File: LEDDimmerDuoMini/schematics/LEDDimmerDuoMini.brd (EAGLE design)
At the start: 84.8 x 27.9 mm, 17 parts, among them IC1 7805T, T1 2N3904, T2 2N3904

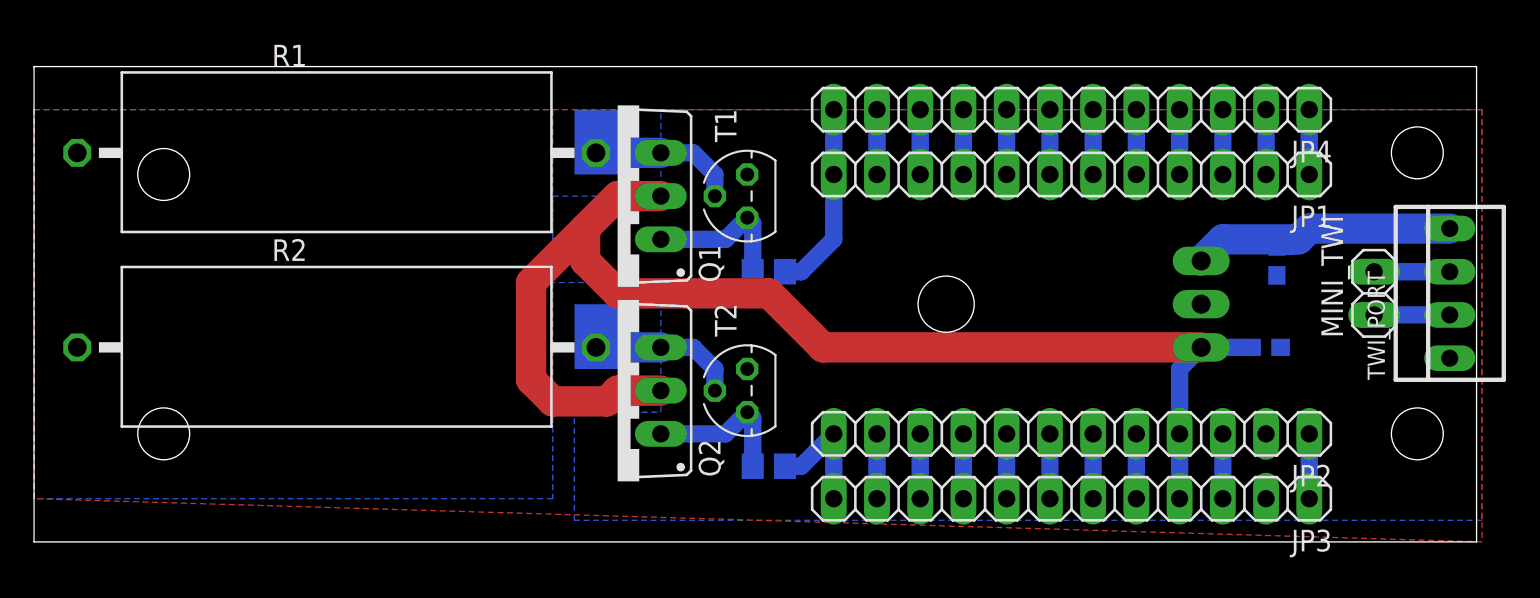
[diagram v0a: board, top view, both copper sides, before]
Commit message: Fixed faulty scematic for LEDDimmerDuoMini
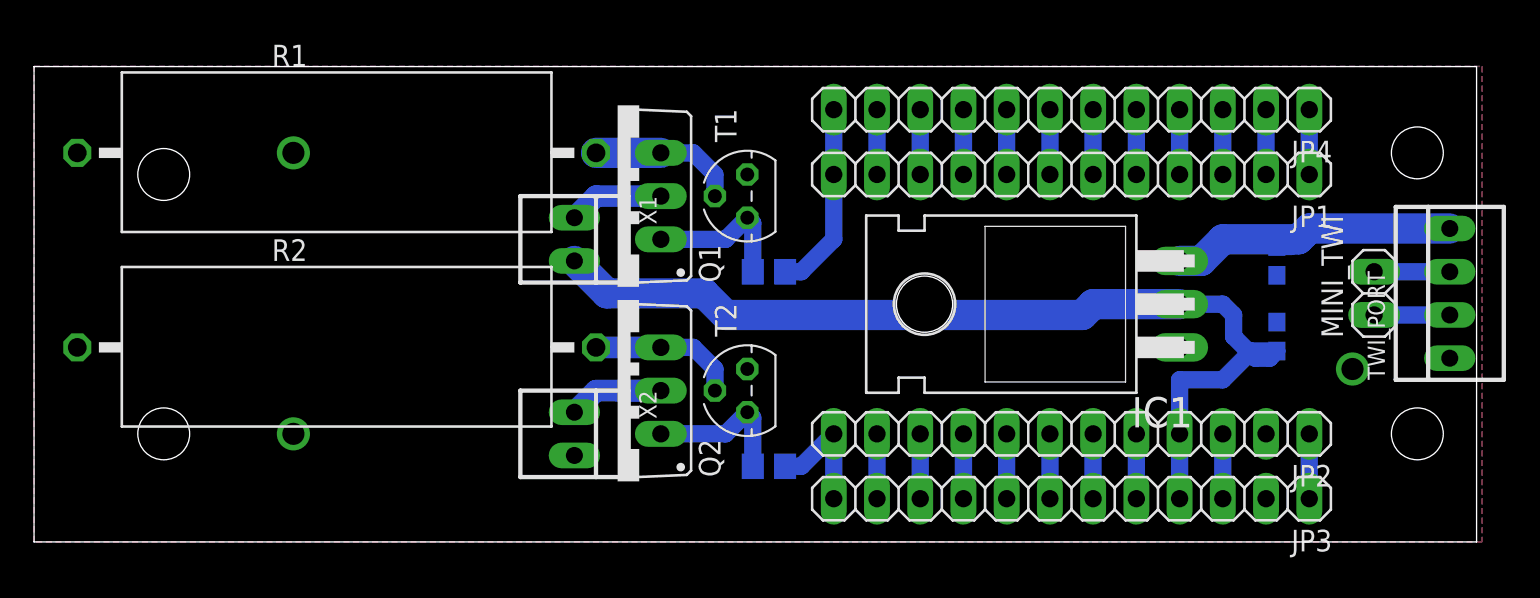
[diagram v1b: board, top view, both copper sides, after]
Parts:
- added X1, X2: 22-23-2021, con-molex:22-23-2021
- IC1: device adafruit:TO220H -> linear:TO220H
- moved IC1 1.27 mm to (57.1, 14.0), flipped to the top, turned to 90 degrees
- moved C3 0.90 mm to (73.0, 12.1), turned to 90 degrees
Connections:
- new net N$26: Q1.D, X1.1
- new net N$27: Q2.D, X2.1
- net +12V: now also IC1.3; no longer IC1.1
- net 5V: now also IC1.2, X1.2; no longer IC1.3, Q1.D, Q2.D
- net GND: now also IC1.1; no longer IC1.2
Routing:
- net 5V: track 76.4 -> 58.5 mm
- net N$27: track 0.00 -> 8.15 mm
- net N$26: track 0.00 -> 5.61 mm
- net +12V: track 17.3 -> 18.6 mm
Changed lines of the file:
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@@
 <hole x="7.62" y="6.35" drill="3.048"/>
 <hole x="7.62" y="21.59" drill="3.048"/>
-<rectangle x1="31.75" y1="21.59" x2="34.29" y2="25.4" layer="16"/>
-<rectangle x1="31.75" y1="10.16" x2="34.29" y2="13.97" layer="16"/>
 </plain>
 <attributes>
@@
 </autorouter>
 <elements>
-<element name="IC1" library="adafruit" package="TO220H" value="7805T" x="58.42" y="13.97" rot="MR270"/>
 <element name="C2" library="SparkFun-Capacitors" package="0603-CAP" value="" x="73.025" y="16.51" rot="MR270"/>
-<element name="C3" library="SparkFun-Capacitors" package="0603-CAP" value="" x="72.39" y="11.43" rot="MR180"/>
+<element name="C3" library="SparkFun-Capacitors" package="0603-CAP" value="" x="73.025" y="12.065" rot="MR90"/>
 <element name="JP1" library="pinhead" package="1X12" value="" x="60.96" y="21.59" rot="R180"/>
 <element name="JP2" library="pinhead" package="1X12" value="" x="60.96" y="6.35" rot="R180"/>
@@
 <element name="JP3" library="pinhead" package="1X12" value="" x="60.96" y="2.54" rot="R180"/>
 <element name="JP4" library="pinhead" package="1X12" value="" x="60.96" y="25.4" rot="R180"/>
+<element name="X1" library="con-molex" package="22-23-2021" value="22-23-2021" x="31.75" y="17.78" rot="R270">
+<attribute name="OC_NEWARK" value="25C3832" x="31.75" y="17.78" size="1.778" layer="27" rot="R270" display="off"/>
+<attribute name="MPN" value="22-23-2021" x="31.75" y="17.78" size="1.778" layer="27" rot="R270" display="off"/>
+<attribute name="MF" value="MOLEX" x="31.75" y="17.78" size="1.778" layer="27" rot="R270" display="off"/>
+<attribute name="OC_FARNELL" value="1462926" x="31.75" y="17.78" size="1.778" layer="27" rot="R270" display="off"/>
+</element>
+<element name="X2" library="con-molex" package="22-23-2021" value="22-23-2021" x="31.75" y="6.35" rot="R270">
+<attribute name="OC_NEWARK" value="25C3832" x="31.75" y="6.35" size="1.778" layer="27" rot="R270" display="off"/>
+<attribute name="MPN" value="22-23-2021" x="31.75" y="6.35" size="1.778" layer="27" rot="R270" display="off"/>
+<attribute name="MF" value="MOLEX" x="31.75" y="6.35" size="1.778" layer="27" rot="R270" display="off"/>
+<attribute name="OC_FARNELL" value="1462926" x="31.75" y="6.35" size="1.778" layer="27" rot="R270" display="off"/>
+</element>
+<element name="IC1" library="linear" package="TO220H" value="7805T" x="57.15" y="13.97" rot="R90"/>
 </elements>
 <signals>
 <signal name="GND">
-<contactref element="IC1" pad="2"/>
 <contactref element="C2" pad="2"/>
 <contactref element="C3" pad="2"/>
@@
 <contactref element="R2" pad="1"/>
 <contactref element="T2" pad="1"/>
-<polygon width="1.016" layer="16">
-<vertex x="0" y="25.4"/>
-<vertex x="30.48" y="25.4"/>
-<vertex x="30.48" y="2.54"/>
-<vertex x="0" y="2.54"/>
+<contactref element="JP3" pad="2"/>
+<polygon width="1.016" layer="1">
+<vertex x="0" y="27.94"/>
+<vertex x="85.09" y="27.94"/>
+<vertex x="85.09" y="0"/>
+<vertex x="0" y="0"/>
 </polygon>
 <polygon width="1.016" layer="16">
-<vertex x="30.48" y="20.32"/>
-<vertex x="36.83" y="20.32"/>
-<vertex x="36.83" y="25.4"/>
-<vertex x="85.09" y="25.4"/>
-<vertex x="85.09" y="1.27"/>
-<vertex x="31.75" y="1.27"/>
-<vertex x="31.75" y="7.62"/>
-<vertex x="36.83" y="7.62"/>
-<vertex x="36.83" y="15.24"/>
-<vertex x="30.48" y="15.24"/>
+<vertex x="0" y="27.94"/>
+<vertex x="85.09" y="27.94"/>
+<vertex x="85.09" y="0"/>
+<vertex x="0" y="0"/>
 </polygon>
-<polygon width="1.016" layer="1">
-<vertex x="0" y="25.4"/>
-<vertex x="85.09" y="25.4"/>
-<vertex x="85.09" y="0"/>
-<vertex x="0" y="2.54"/>
-</polygon>
-<contactref element="JP3" pad="2"/>
+<contactref element="IC1" pad="1"/>
 </signal>
 <signal name="+12V">
-<contactref element="IC1" pad="1"/>
 <contactref element="C2" pad="1"/>
 <contactref element="TWI_PORT" pad="4"/>
-<wire x1="68.58" y1="16.51" x2="69.85" y2="17.78" width="1.778" layer="16"/>
 <wire x1="69.85" y1="17.78" x2="74.295" y2="17.78" width="1.778" layer="16"/>
 <wire x1="74.295" y1="17.78" x2="74.6125" y2="18.0975" width="1.778" layer="16"/>
@@
 <wire x1="73.025" y1="17.36" x2="73.875" y2="17.36" width="1.016" layer="16"/>
 <wire x1="73.875" y1="17.36" x2="74.6125" y2="18.0975" width="1.016" layer="16"/>
+<contactref element="IC1" pad="3"/>
+<wire x1="69.85" y1="17.78" x2="68.58" y2="16.51" width="1.778" layer="16"/>
+<wire x1="68.58" y1="16.51" x2="67.31" y2="16.51" width="1.778" layer="16"/>
 </signal>
 <signal name="INB">
@@
 <signal name="5V">
 <contactref element="JP2" pad="4"/>
-<contactref element="IC1" pad="3"/>
 <contactref element="C3" pad="1"/>
-<contactref element="Q1" pad="D"/>
-<contactref element="Q2" pad="D"/>
-<wire x1="68.58" y1="11.43" x2="67.31" y2="10.16" width="1.016" layer="16"/>
-<wire x1="67.31" y1="10.16" x2="67.31" y2="6.35" width="1.016" layer="16"/>
-<wire x1="68.58" y1="11.43" x2="46.355" y2="11.43" width="1.778" layer="1"/>
-<wire x1="46.355" y1="11.43" x2="43.18" y2="14.605" width="1.778" layer="1"/>
-<wire x1="43.18" y1="14.605" x2="34.29" y2="14.605" width="1.778" layer="1"/>
-<wire x1="34.29" y1="14.605" x2="32.385" y2="16.51" width="1.778" layer="1"/>
-<wire x1="32.385" y1="16.51" x2="32.385" y2="18.415" width="1.778" layer="1"/>
-<wire x1="32.385" y1="18.415" x2="34.29" y2="20.32" width="1.778" layer="1"/>
-<wire x1="34.29" y1="20.32" x2="36.83" y2="20.32" width="1.778" layer="1"/>
-<wire x1="36.83" y1="8.89" x2="34.29" y2="8.89" width="1.778" layer="1"/>
-<wire x1="34.29" y1="8.89" x2="33.655" y2="8.255" width="1.778" layer="1"/>
-<wire x1="33.655" y1="8.255" x2="30.48" y2="8.255" width="1.778" layer="1"/>
-<wire x1="30.48" y1="8.255" x2="29.21" y2="9.525" width="1.778" layer="1"/>
-<wire x1="29.21" y1="9.525" x2="29.21" y2="15.24" width="1.778" layer="1"/>
-<wire x1="29.21" y1="15.24" x2="32.385" y2="18.415" width="1.778" layer="1"/>
-<wire x1="68.58" y1="11.43" x2="71.54" y2="11.43" width="1.016" layer="16"/>
 <contactref element="JP3" pad="4"/>
 <wire x1="67.31" y1="2.54" x2="67.31" y2="6.35" width="1.016" layer="16"/>
+<contactref element="X1" pad="2"/>
+<contactref element="IC1" pad="2"/>
+<wire x1="31.75" y1="16.51" x2="33.655" y2="14.605" width="1.778" layer="16"/>
+<wire x1="33.655" y1="14.605" x2="39.37" y2="14.605" width="1.778" layer="16"/>
+<wire x1="39.37" y1="14.605" x2="40.64" y2="13.335" width="1.778" layer="16"/>
+<wire x1="40.64" y1="13.335" x2="61.595" y2="13.335" width="1.778" layer="16"/>
+<wire x1="61.595" y1="13.335" x2="62.23" y2="13.97" width="1.778" layer="16"/>
+<wire x1="62.23" y1="13.97" x2="67.31" y2="13.97" width="1.778" layer="16"/>
+<wire x1="67.31" y1="13.97" x2="69.85" y2="13.97" width="1.016" layer="16"/>
+<wire x1="69.85" y1="13.97" x2="70.485" y2="13.335" width="1.016" layer="16"/>
+<wire x1="70.485" y1="13.335" x2="70.485" y2="12.065" width="1.016" layer="16"/>
+<wire x1="70.485" y1="12.065" x2="71.755" y2="10.795" width="1.016" layer="16"/>
+<wire x1="71.755" y1="10.795" x2="72.605" y2="10.795" width="1.016" layer="16"/>
+<wire x1="72.605" y1="10.795" x2="73.025" y2="11.215" width="1.016" layer="16"/>
+<wire x1="73.025" y1="11.215" x2="71.54" y2="11.215" width="1.016" layer="16"/>
+<wire x1="71.54" y1="11.215" x2="69.85" y2="9.525" width="1.016" layer="16"/>
+<wire x1="69.85" y1="9.525" x2="67.31" y2="9.525" width="1.016" layer="16"/>
+<wire x1="67.31" y1="9.525" x2="67.31" y2="6.35" width="1.016" layer="16"/>
 </signal>
 <signal name="RX">
@@
 <wire x1="38.735" y1="11.43" x2="40.005" y2="10.16" width="1.016" layer="16"/>
 <wire x1="40.005" y1="10.16" x2="40.005" y2="8.89" width="1.016" layer="16"/>
-<wire x1="33.02" y1="11.43" x2="36.83" y2="11.43" width="1.778" layer="16"/>
+<wire x1="36.83" y1="11.43" x2="33.02" y2="11.43" width="1.27" layer="16"/>
 </signal>
 <signal name="N$7">
@@
 <wire x1="49.53" y1="6.35" x2="49.53" y2="2.54" width="1.016" layer="16"/>
 </signal>
+<signal name="N$26">
+<contactref element="Q1" pad="D"/>
+<contactref element="X1" pad="1"/>
+<wire x1="31.75" y1="19.05" x2="33.02" y2="20.32" width="1.27" layer="16"/>
+<wire x1="33.02" y1="20.32" x2="36.83" y2="20.32" width="1.27" layer="16"/>
+</signal>
+<signal name="N$27">
+<contactref element="Q2" pad="D"/>
+<wire x1="34.29" y1="8.89" x2="36.83" y2="8.89" width="1.27" layer="16"/>
+<contactref element="X2" pad="1"/>
+<wire x1="31.75" y1="7.62" x2="33.02" y2="8.89" width="1.27" layer="16"/>
+<wire x1="33.02" y1="8.89" x2="36.83" y2="8.89" width="1.27" layer="16"/>
+</signal>
+<signal name="N$29">
+<via x="15.24" y="22.86" extent="1-16" drill="1.3" shape="square"/>
+</signal>
+<signal name="N$30">
+<via x="15.24" y="6.35" extent="1-16" drill="1.3" shape="square"/>
+</signal>
+<signal name="N$31">
+<via x="77.47" y="10.16" extent="1-16" drill="1.3" shape="square"/>
+</signal>
 </signals>

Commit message: HOK post laptop update
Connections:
- net GND: now also X2.2
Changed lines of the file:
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@@
 </polygon>
 <contactref element="IC1" pad="1"/>
+<via x="15.24" y="22.86" extent="1-16" drill="1.3" shape="square"/>
+<via x="15.24" y="6.35" extent="1-16" drill="1.3" shape="square"/>
+<via x="78.74" y="2.54" extent="1-16" drill="1.3" shape="square"/>
+<contactref element="X2" pad="2"/>
 </signal>
 <signal name="+12V">
@@
 <wire x1="33.02" y1="8.89" x2="36.83" y2="8.89" width="1.27" layer="16"/>
 </signal>
-<signal name="N$29">
-<via x="15.24" y="22.86" extent="1-16" drill="1.3" shape="square"/>
-</signal>
-<signal name="N$30">
-<via x="15.24" y="6.35" extent="1-16" drill="1.3" shape="square"/>
-</signal>
-<signal name="N$31">
-<via x="77.47" y="10.16" extent="1-16" drill="1.3" shape="square"/>
-</signal>
 </signals>
